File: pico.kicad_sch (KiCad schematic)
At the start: 31 parts, among them J1 10103594-0001LF, J5 TSW-102-07-G-S, SW5 SW_boot, U4 NCP1117ST33T3G, U5 W25Q128JVSIQ, U6 RP2040, U7 W25Q128JVSIQ, X1 12MHz

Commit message: Últimos cambios: referencias Arial, clearances net classes, vias 0.6mm
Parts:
- added L1: 100mH, Resistor_SMD:R_2512_6332Metric, symbol Device:L
- C10, C11, C13, C17, C24, C3, C5: footprint Capacitor_SMD:C_0805_2012Metric -> Capacitor_SMD:C_0603_1608Metric
- C9: footprint RaspberryPI PicoW:generic_capc2012x125 -> Capacitor_SMD:C_0603_1608Metric
- R12: footprint Resistor_SMD:R_0805_2012Metric -> Resistor_SMD:R_0603_1608Metric
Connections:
- net VBUS: now also L1.1; no longer C6.1, U4.3 (IN)
- new net: C6.1, L1.2, U4.3 (IN)
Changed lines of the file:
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@@
 	)
 	(junction
+		(at 66.04 55.88)
+		(diameter 0)
+		(color 0 0 0 0)
+	)
+	(junction
 		(at 52.07 242.57)
 		(diameter 0)
@@
 	)
 	(junction
-		(at 66.04 55.88)
-		(diameter 0)
-		(color 0 0 0 0)
-	)
-	(junction
 		(at 307.34 62.23)
 		(diameter 0)
@@
 	(wire
 		(pts
+			(xy 57.15 55.88) (xy 55.88 55.88)
+		)
+		(stroke
+			(width 0)
+			(type default)
+		)
+	)
+	(wire
+		(pts
 			(xy 311.15 171.45) (xy 317.5 171.45)
 		)
@@
 	(wire
 		(pts
-			(xy 55.88 55.88) (xy 66.04 55.88)
-		)
-		(stroke
-			(width 0)
-			(type default)
-		)
-	)
-	(wire
-		(pts
 			(xy 242.57 48.26) (xy 254 48.26)
 		)
@@
 	(wire
 		(pts
+			(xy 64.77 55.88) (xy 66.04 55.88)
+		)
+		(stroke
+			(width 0)
+			(type default)
+		)
+	)
+	(wire
+		(pts
 			(xy 71.12 137.16) (xy 97.79 137.16)
 		)
@@
 			)
 		)
-		(property "Footprint" "RaspberryPI PicoW:generic_capc2012x125"
+		(property "Footprint" "Capacitor_SMD:C_0603_1608Metric"
 			(at 105.41 62.23 0)
 			(hide yes)
@@
 			)
 		)
-		(property "Footprint" "Capacitor_SMD:C_0805_2012Metric"
+		(property "Footprint" "Capacitor_SMD:C_0603_1608Metric"
 			(at 254 80.01 0)
 			(hide yes)
@@
 			)
 		)
-		(property "Footprint" "Capacitor_SMD:C_0805_2012Metric"
+		(property "Footprint" "Capacitor_SMD:C_0603_1608Metric"
 			(at 59.69 219.71 0)
 			(hide yes)
@@
 	)
 	(symbol
+		(lib_id "Device:L")
+		(at 60.96 55.88 90)
+		(unit 1)
+		(body_style 1)
+		(exclude_from_sim no)
+		(in_bom yes)
+		(on_board yes)
+		(in_pos_files yes)
+		(dnp no)
+		(fields_autoplaced yes)
+		(property "Reference" "L1"
+			(at 60.96 50.8 90)
+			(show_name no)
+			(do_not_autoplace no)
+			(effects
+				(font
+					(size 1.27 1.27)
+				)
+			)
+		)
+		(property "Value" "100mH"
+			(at 60.96 53.34 90)
+			(show_name no)
+			(do_not_autoplace no)
+			(effects
+				(font
+					(size 1.27 1.27)
+				)
+			)
+		)
+		(property "Footprint" "Resistor_SMD:R_2512_6332Metric"
+			(at 60.96 55.88 0)
+			(hide yes)
+			(show_name no)
+			(do_not_autoplace no)
+			(effects
+				(font
+					(size 1.27 1.27)
+				)
+			)
+		)
+		(property "Datasheet" ""
+			(at 60.96 55.88 0)
+			(hide yes)
+			(show_name no)
+			(do_not_autoplace no)
+			(effects
+				(font
+					(size 1.27 1.27)
+				)
+			)
+		)
+		(property "Description" "Inductor"
+			(at 60.96 55.88 0)
+			(hide yes)
+			(show_name no)
+			(do_not_autoplace no)
+			(effects
+				(font
+					(size 1.27 1.27)
+				)
+			)
+		)
+		(pin "1"
+		)
+		(pin "2"
+		)
+		(instances
+			(project "picow_vga_sd_aud"
+				(path "/7e7c068a-a341-4358-ab45-53bb7a793d6f/356ef146-de37-4728-841c-0ab71def169b"
+					(reference "L1")
+					(unit 1)
+				)
+			)
+		)
+	)
+	(symbol
 		(lib_id "RPI_DB:Capacitors | MLCC | M2012/RP-01GYSK-AVBE41")
 		(at 359.41 204.47 0)
@@
 			)
 		)
-		(property "Footprint" "Capacitor_SMD:C_0805_2012Metric"
+		(property "Footprint" "Capacitor_SMD:C_0603_1608Metric"
 			(at 273.05 80.01 0)
 			(hide yes)
@@
 			)
 		)
-		(property "Footprint" "Capacitor_SMD:C_0805_2012Metric"
+		(property "Footprint" "Capacitor_SMD:C_0603_1608Metric"
 			(at 125.73 121.92 0)
 			(hide yes)
@@
 			)
 		)
-		(property "Footprint" "Resistor_SMD:R_0805_2012Metric"
+		(property "Footprint" "Resistor_SMD:R_0603_1608Metric"
 			(at 91.44 238.76 0)
 			(hide yes)
@@
 			)
 		)
-		(property "Footprint" "Capacitor_SMD:C_0805_2012Metric"
+		(property "Footprint" "Capacitor_SMD:C_0603_1608Metric"
 			(at 242.57 54.61 0)
 			(hide yes)
@@
 			)
 		)
-		(property "Footprint" "Capacitor_SMD:C_0805_2012Metric"
+		(property "Footprint" "Capacitor_SMD:C_0603_1608Metric"
 			(at 59.69 242.57 0)
 			(hide yes)
@@
 			)
 		)
-		(property "Footprint" "Capacitor_SMD:C_0805_2012Metric"
+		(property "Footprint" "Capacitor_SMD:C_0603_1608Metric"
 			(at 341.63 54.61 0)
 			(hide yes)

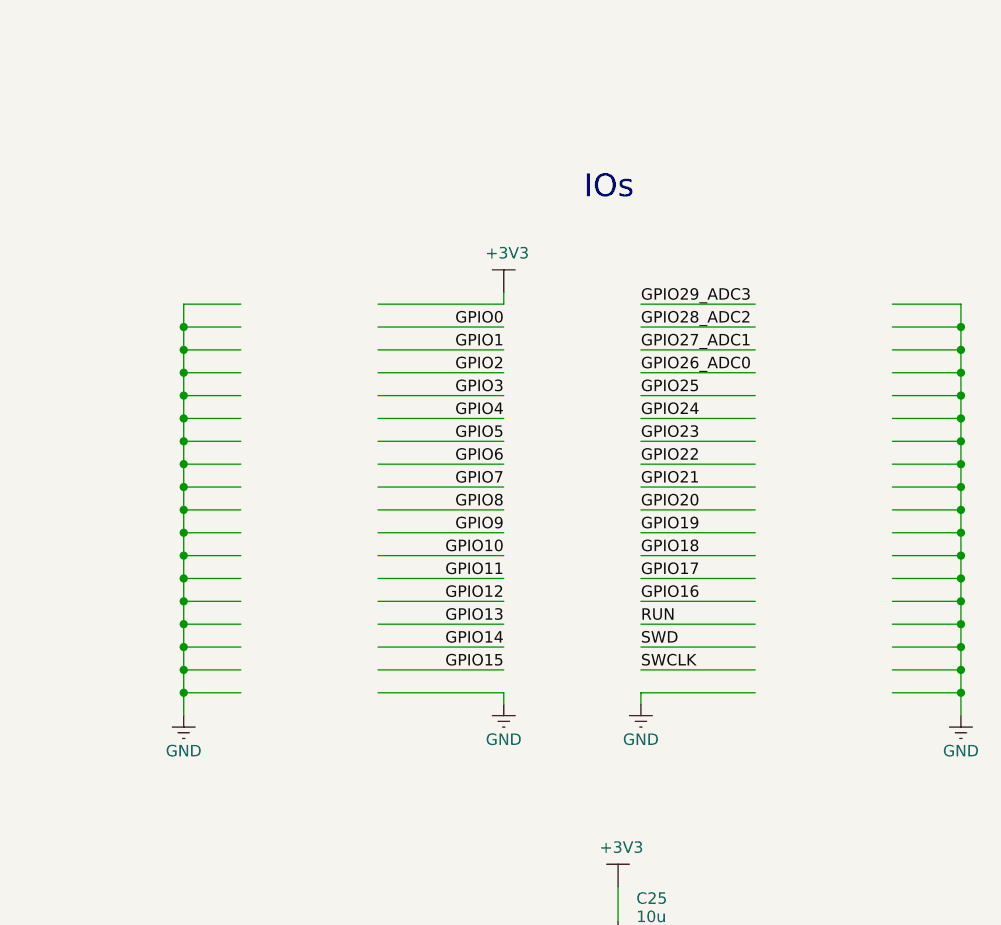
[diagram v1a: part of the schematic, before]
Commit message: Actualizar archivos del proyecto KiCad
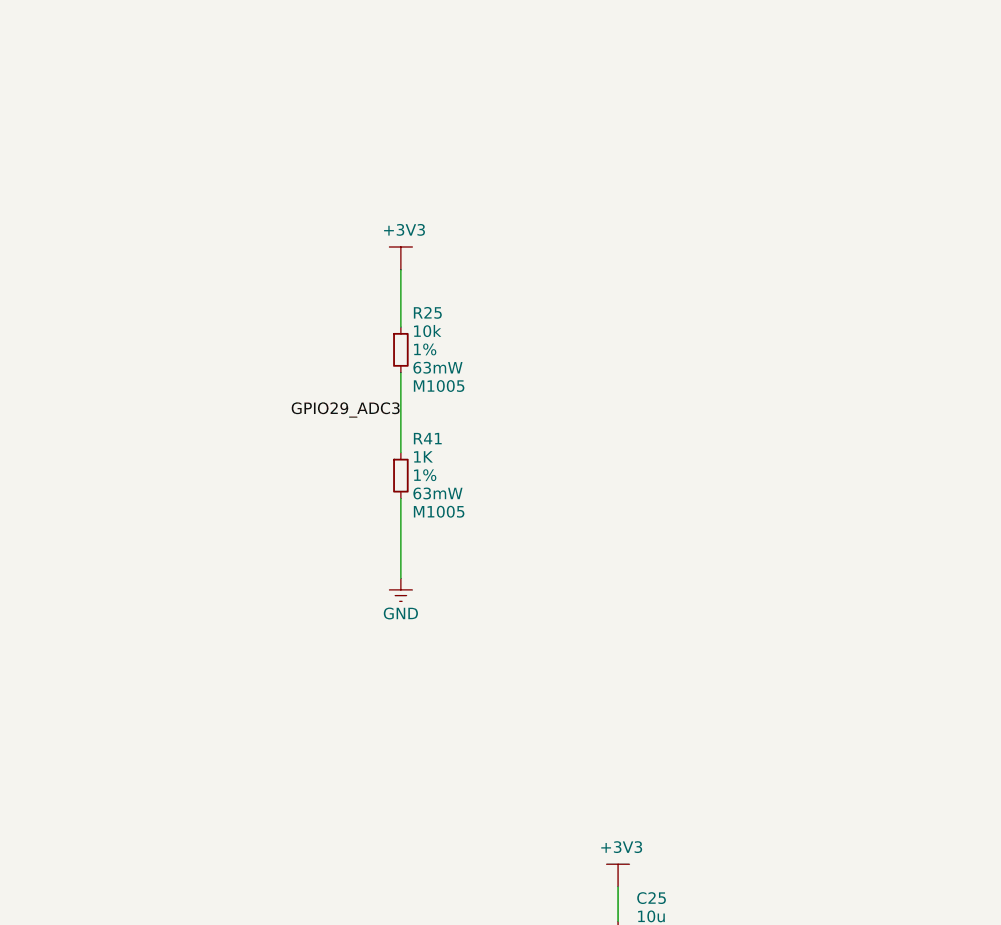
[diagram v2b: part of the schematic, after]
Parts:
- added R25: 10k, Resistor_SMD:R_0603_1608Metric, symbol RPI_DB:Resistors | Chip | M1005/RP-01C89V-LTEYC4
- added R41: 1K, Resistor_SMD:R_0603_1608Metric, symbol RPI_DB:Resistors | Chip | M1005/RP-01C89V-LTEYC4
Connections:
- net +3V3: now also R25.1
- net GND: now also R41.2
- net GPIO29_ADC3: now also R25.2, R41.1
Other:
- note removed: "IOs"

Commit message: Update schematics and PCB
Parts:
- C18, J5, R25, R41, U5: now left out of the parts list
- C25, C6: footprint RaspberryPI PicoW:generic_capc2012x125 -> Capacitor_SMD:C_0805_2012Metric
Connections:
- net +3V3: no longer U4.4 (OUT)
- no-connect marks 1 -> 2
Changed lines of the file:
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@@
 	)
 	(junction
-		(at 95.25 54.61)
-		(diameter 0)
-		(color 0 0 0 0)
-	)
-	(junction
 		(at 71.12 137.16)
 		(diameter 0)
@@
 	)
 	(junction
-		(at 105.41 54.61)
-		(diameter 0)
-		(color 0 0 0 0)
-	)
-	(junction
 		(at 119.38 116.84)
 		(diameter 0)
@@
 	)
 	(junction
-		(at 55.88 55.88)
-		(diameter 0)
-		(color 0 0 0 0)
-	)
-	(junction
 		(at 254 48.26)
 		(diameter 0)
@@
 	)
 	(junction
+		(at 69.85 55.88)
+		(diameter 0)
+		(color 0 0 0 0)
+	)
+	(junction
 		(at 35.56 77.47)
 		(diameter 0)
@@
 	)
 	(junction
+		(at 105.41 57.15)
+		(diameter 0)
+		(color 0 0 0 0)
+	)
+	(junction
 		(at 242.57 62.23)
 		(diameter 0)
@@
 	)
 	(junction
+		(at 55.88 55.88)
+		(diameter 0)
+		(color 0 0 0 0)
+	)
+	(junction
 		(at 284.48 48.26)
 		(diameter 0)
@@
 		(at 44.45 63.5)
 	)
+	(no_connect
+		(at 92.71 54.61)
+	)
 	(wire
 		(pts
@@
 	(wire
 		(pts
-			(xy 105.41 54.61) (xy 105.41 59.69)
-		)
-		(stroke
-			(width 0)
-			(type default)
-		)
-	)
-	(wire
-		(pts
 			(xy 78.74 153.67) (xy 97.79 153.67)
 		)
@@
 	(wire
 		(pts
-			(xy 92.71 57.15) (xy 95.25 57.15)
+			(xy 92.71 57.15) (xy 105.41 57.15)
 		)
 		(stroke
@@
 	(wire
 		(pts
-			(xy 95.25 57.15) (xy 95.25 54.61)
-		)
-		(stroke
-			(width 0)
-			(type default)
-		)
-	)
-	(wire
-		(pts
 			(xy 199.39 186.69) (xy 199.39 203.2)
 		)
@@
 	(wire
 		(pts
+			(xy 105.41 57.15) (xy 105.41 59.69)
+		)
+		(stroke
+			(width 0)
+			(type default)
+		)
+	)
+	(wire
+		(pts
 			(xy 359.41 198.12) (xy 359.41 201.93)
 		)
@@
 	(wire
 		(pts
-			(xy 273.05 48.26) (xy 284.48 48.26)
+			(xy 69.85 55.88) (xy 74.93 55.88)
 		)
 		(stroke
@@
 	(wire
 		(pts
-			(xy 191.77 111.76) (xy 191.77 125.73)
+			(xy 273.05 48.26) (xy 284.48 48.26)
 		)
 		(stroke
@@
 	(wire
 		(pts
-			(xy 105.41 64.77) (xy 105.41 67.31)
+			(xy 191.77 111.76) (xy 191.77 125.73)
 		)
 		(stroke
@@
 	(wire
 		(pts
-			(xy 95.25 54.61) (xy 105.41 54.61)
+			(xy 105.41 64.77) (xy 105.41 67.31)
 		)
 		(stroke
@@
 	(wire
 		(pts
-			(xy 105.41 53.34) (xy 105.41 54.61)
+			(xy 105.41 53.34) (xy 105.41 57.15)
 		)
 		(stroke
@@
 	(wire
 		(pts
-			(xy 55.88 54.61) (xy 55.88 55.88)
+			(xy 55.88 48.26) (xy 55.88 55.88)
 		)
 		(stroke
@@
 	(wire
 		(pts
-			(xy 66.04 55.88) (xy 74.93 55.88)
+			(xy 66.04 55.88) (xy 69.85 55.88)
 		)
 		(stroke
@@
 	(wire
 		(pts
-			(xy 92.71 54.61) (xy 95.25 54.61)
-		)
-		(stroke
-			(width 0)
-			(type default)
-		)
-	)
-	(wire
-		(pts
 			(xy 236.22 144.78) (xy 251.46 144.78)
 		)
@@
 	(symbol
 		(lib_id "RPI - Power:PWR_NET")
-		(at 55.88 54.61 0)
+		(at 55.88 48.26 0)
 		(unit 1)
 		(body_style 1)
@@
 		(dnp no)
 		(property "Reference" "#PWR03"
-			(at 55.88 58.42 0)
+			(at 55.88 52.07 0)
 			(hide yes)
 			(show_name no)
@@
 		)
 		(property "Value" "VBUS"
-			(at 56.261 50.2158 0)
+			(at 56.261 43.8658 0)
 			(show_name no)
 			(do_not_autoplace no)
@@
 		)
 		(property "Footprint" ""
-			(at 55.88 54.61 0)
+			(at 55.88 48.26 0)
 			(hide yes)
 			(show_name no)
@@
 		)
 		(property "Datasheet" ""
-			(at 55.88 54.61 0)
+			(at 55.88 48.26 0)
 			(hide yes)
 			(show_name no)
@@
 		)
 		(property "Description" ""
-			(at 55.88 54.61 0)
+			(at 55.88 48.26 0)
 			(hide yes)
 			(show_name no)
@@
 	)
 	(symbol
+		(lib_id "power:PWR_FLAG")
+		(at 69.85 55.88 0)
+		(unit 1)
+		(body_style 1)
+		(exclude_from_sim no)
+		(in_bom yes)
+		(on_board yes)
+		(in_pos_files yes)
+		(dnp no)
+		(fields_autoplaced yes)
+		(property "Reference" "#FLG01"
+			(at 69.85 53.975 0)
+			(hide yes)
+			(show_name no)
+			(do_not_autoplace no)
+			(effects
+				(font
+					(size 1.27 1.27)
+				)
+			)
+		)
+		(property "Value" "PWR_FLAG"
+			(at 69.85 50.8 0)
+			(show_name no)
+			(do_not_autoplace no)
+			(effects
+				(font
+					(size 1.27 1.27)
+				)
+			)
+		)
+		(property "Footprint" ""
+			(at 69.85 55.88 0)
+			(hide yes)
+			(show_name no)
+			(do_not_autoplace no)
+			(effects
+				(font
+					(size 1.27 1.27)
+				)
+			)
+		)
+		(property "Datasheet" ""
+			(at 69.85 55.88 0)
+			(hide yes)
+			(show_name no)
+			(do_not_autoplace no)
+			(effects
+				(font
+					(size 1.27 1.27)
+				)
+			)
+		)
+		(property "Description" "Special symbol for telling ERC where power comes from"
+			(at 69.85 55.88 0)
+			(hide yes)
+			(show_name no)
+			(do_not_autoplace no)
+			(effects
+				(font
+					(size 1.27 1.27)
+				)
+			)
+		)
+		(pin "1"
+		)
+		(instances
+			(project "picow_vga_sd_aud"
+				(path "/7e7c068a-a341-4358-ab45-53bb7a793d6f/356ef146-de37-4728-841c-0ab71def169b"
+					(reference "#FLG01")
+					(unit 1)
+				)
+			)
+		)
+	)
+	(symbol
 		(lib_id "RPI - Power:GND")
 		(at 48.26 166.37 0)
@@
 		(body_style 1)
 		(exclude_from_sim no)
-		(in_bom yes)
+		(in_bom no)
 		(on_board yes)
-		(in_pos_files yes)
+		(in_pos_files no)
 		(dnp no)
 		(property "Reference" "C18"
@@
 			)
 		)
-		(property "Footprint" "RaspberryPI PicoW:generic_capc2012x125"
+		(property "Footprint" "Capacitor_SMD:C_0805_2012Metric"
 			(at 359.41 204.47 0)
 			(hide yes)
@@
 		(body_style 1)
 		(exclude_from_sim no)
-		(in_bom yes)
+		(in_bom no)
 		(on_board yes)
-		(in_pos_files yes)
+		(in_pos_files no)
 		(dnp no)
 		(property "Reference" "U5"
@@
 			)
 		)
-		(property "Footprint" "RaspberryPI PicoW:generic_capc2012x125"
+		(property "Footprint" "Capacitor_SMD:C_0805_2012Metric"
 			(at 66.04 63.5 0)
 			(hide yes)
@@
 		(body_style 1)
 		(exclude_from_sim no)
-		(in_bom yes)
+		(in_bom no)
 		(on_board yes)
-		(in_pos_files yes)
+		(in_pos_files no)
 		(dnp no)
 		(property "Reference" "R41"
@@
 		(body_style 1)
 		(exclude_from_sim no)
-		(in_bom yes)
+		(in_bom no)
 		(on_board yes)
-		(in_pos_files yes)
+		(in_pos_files no)
 		(dnp no)
 		(property "Reference" "J5"
@@
 		(body_style 1)
 		(exclude_from_sim no)
-		(in_bom yes)
+		(in_bom no)
 		(on_board yes)
-		(in_pos_files yes)
+		(in_pos_files no)
 		(dnp no)
 		(property "Reference" "R25"
